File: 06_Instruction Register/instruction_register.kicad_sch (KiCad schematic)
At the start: 18 parts, among them U1 74LS377, U2 74LS245

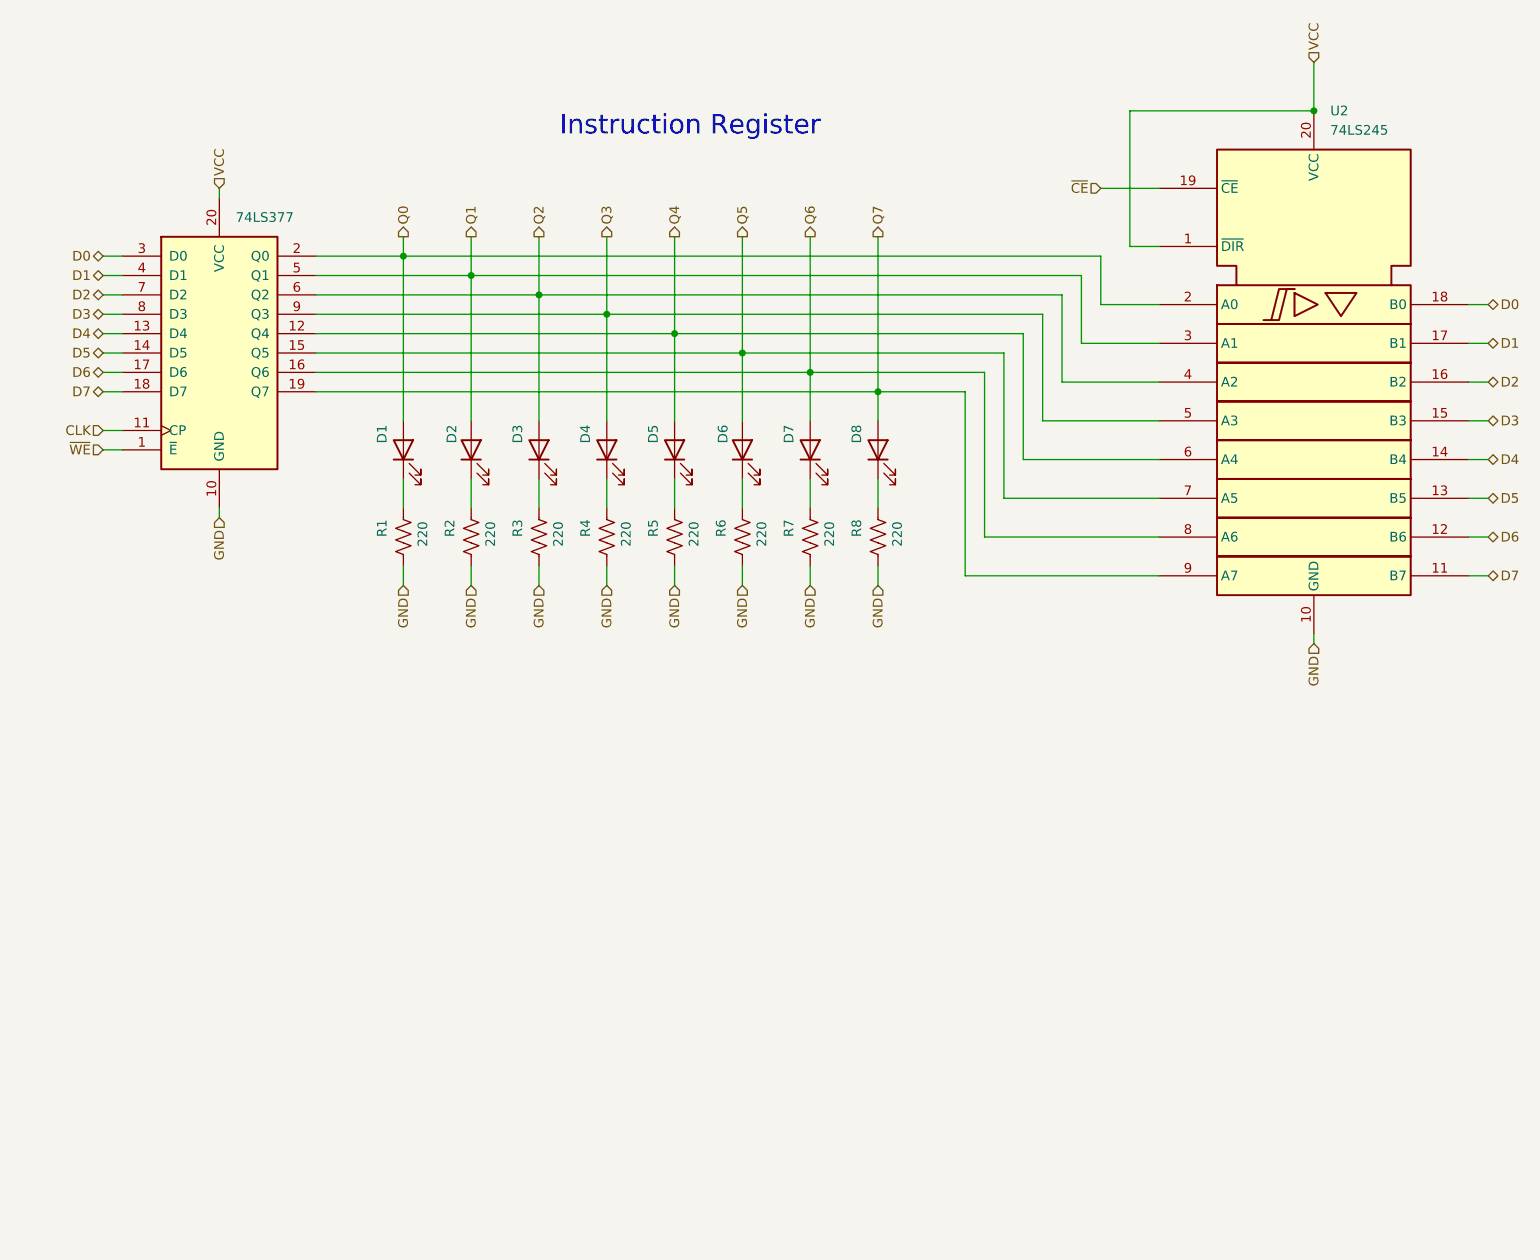
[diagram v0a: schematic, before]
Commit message: Last revision of the cpu, all boards have been ordered. Implementation to be tested and documented in following commits.
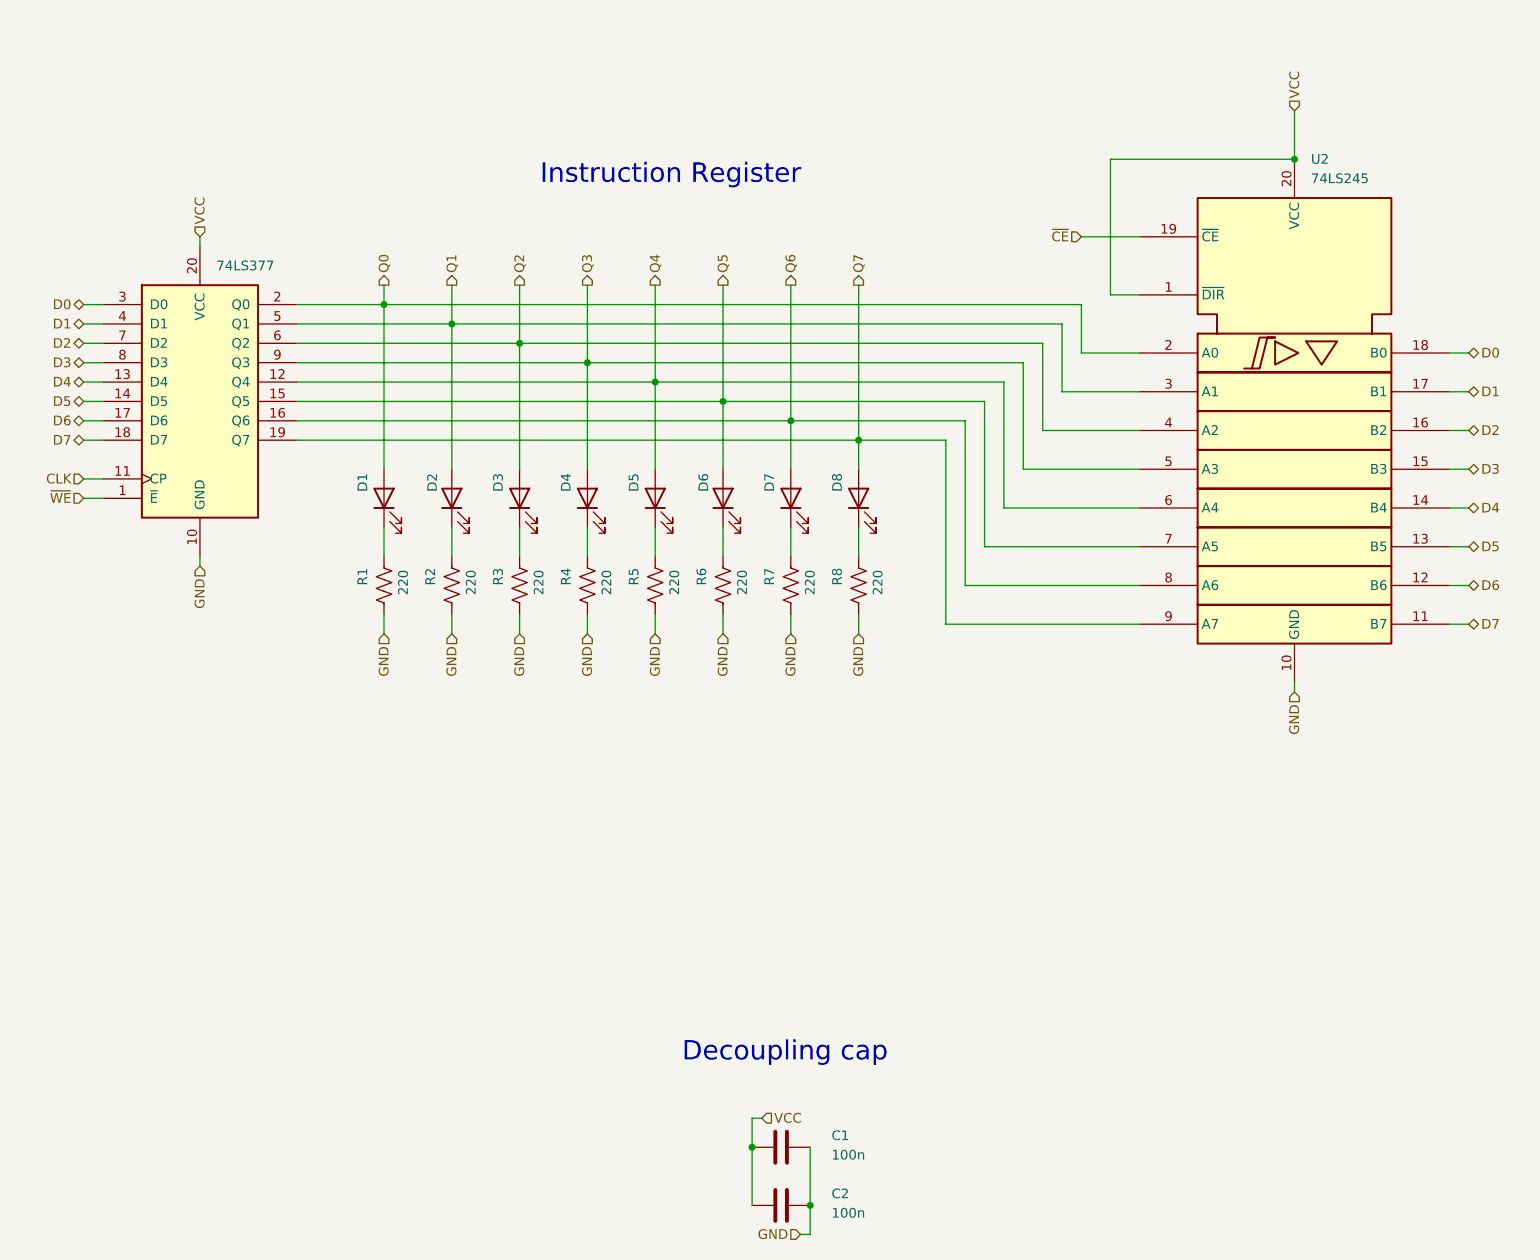
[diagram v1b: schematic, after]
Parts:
- added C1, C2: 100n, Capacitor_THT:C_Disc_D3.0mm_W1.6mm_P2.50mm, symbol Device:C
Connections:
- net GND: now also C1.2, C2.2
- net VCC: now also C1.1, C2.1
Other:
- note added: "Decoupling cap"
- moved on the sheet: D1, D2, D3, D4, D5, D6, D7, D8, R1, R2, R3, R4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
